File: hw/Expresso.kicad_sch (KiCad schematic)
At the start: 4 parts

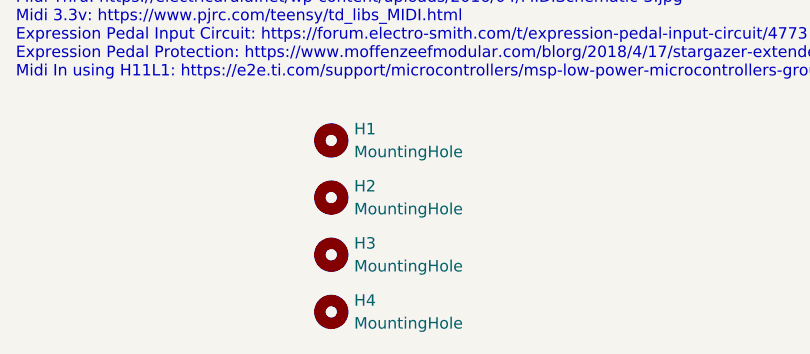
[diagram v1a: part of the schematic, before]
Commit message: added new pcb design, ERC errors not fixed yet
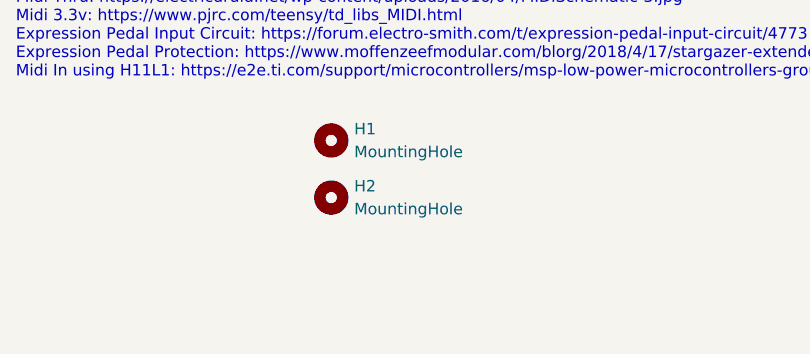
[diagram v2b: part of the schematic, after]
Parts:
- removed H3, H4: MountingHole, MountingHole:MountingHole_3.2mm_M3, symbol Mechanical:MountingHole
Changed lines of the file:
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@@
-	(symbol
-		(lib_id "Mechanical:MountingHole")
-		(at 50.8 190.5 0)
-		(unit 1)
-		(exclude_from_sim no)
-		(in_bom no)
-		(on_board yes)
-		(dnp no)
-		(fields_autoplaced yes)
-		(property "Reference" "H4"
-			(at 53.34 189.2299 0)
-			(effects
-				(font
-					(size 1.27 1.27)
-				)
-				(justify left)
-			)
-		)
-		(property "Value" "MountingHole"
-			(at 53.34 191.7699 0)
-			(effects
-				(font
-					(size 1.27 1.27)
-				)
-				(justify left)
-			)
-		)
-		(property "Footprint" "MountingHole:MountingHole_3.2mm_M3"
-			(at 50.8 190.5 0)
-			(effects
-				(font
-					(size 1.27 1.27)
-				)
-				(hide yes)
-			)
-		)
-		(property "Datasheet" "~"
-			(at 50.8 190.5 0)
-			(effects
-				(font
-					(size 1.27 1.27)
-				)
-				(hide yes)
-			)
-		)
-		(property "Description" "Mounting Hole without connection"
-			(at 50.8 190.5 0)
-			(effects
-				(font
-					(size 1.27 1.27)
-				)
-				(hide yes)
-			)
-		)
-		(instances
-			(project "Midi Expressor"
-				(path "/1e7cbae1-0003-4e27-ba62-2dd55b10f4f2"
-					(reference "H4")
-					(unit 1)
-				)
-			)
-		)
-	)
-	(symbol
-		(lib_id "Mechanical:MountingHole")
-		(at 50.8 184.15 0)
-		(unit 1)
-		(exclude_from_sim no)
-		(in_bom no)
-		(on_board yes)
-		(dnp no)
-		(fields_autoplaced yes)
-		(property "Reference" "H3"
-			(at 53.34 182.8799 0)
-			(effects
-				(font
-					(size 1.27 1.27)
-				)
-				(justify left)
-			)
-		)
-		(property "Value" "MountingHole"
-			(at 53.34 185.4199 0)
-			(effects
-				(font
-					(size 1.27 1.27)
-				)
-				(justify left)
-			)
-		)
-		(property "Footprint" "MountingHole:MountingHole_3.2mm_M3"
-			(at 50.8 184.15 0)
-			(effects
-				(font
-					(size 1.27 1.27)
-				)
-				(hide yes)
-			)
-		)
-		(property "Datasheet" "~"
-			(at 50.8 184.15 0)
-			(effects
-				(font
-					(size 1.27 1.27)
-				)
-				(hide yes)
-			)
-		)
-		(property "Description" "Mounting Hole without connection"
-			(at 50.8 184.15 0)
-			(effects
-				(font
-					(size 1.27 1.27)
-				)
-				(hide yes)
-			)
-		)
-		(instances
-			(project "Midi Expressor"
-				(path "/1e7cbae1-0003-4e27-ba62-2dd55b10f4f2"
-					(reference "H3")
-					(unit 1)
-				)
-			)
-		)
-	)
 	(symbol
 		(lib_id "Mechanical:MountingHole")

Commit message: small PCB updates for casing design
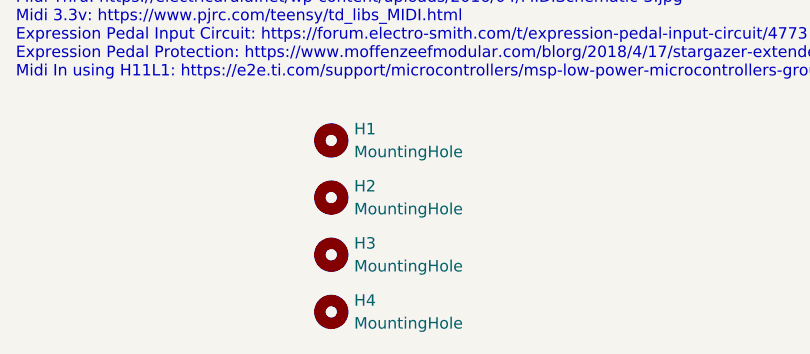
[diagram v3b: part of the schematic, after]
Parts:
- added H3, H4: MountingHole, MountingHole:MountingHole_3.2mm_M3, symbol Mechanical:MountingHole
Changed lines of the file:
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@@
+	(symbol
+		(lib_id "Mechanical:MountingHole")
+		(at 50.8 184.15 0)
+		(unit 1)
+		(exclude_from_sim no)
+		(in_bom no)
+		(on_board yes)
+		(dnp no)
+		(fields_autoplaced yes)
+		(property "Reference" "H3"
+			(at 53.34 182.8799 0)
+			(effects
+				(font
+					(size 1.27 1.27)
+				)
+				(justify left)
+			)
+		)
+		(property "Value" "MountingHole"
+			(at 53.34 185.4199 0)
+			(effects
+				(font
+					(size 1.27 1.27)
+				)
+				(justify left)
+			)
+		)
+		(property "Footprint" "MountingHole:MountingHole_3.2mm_M3"
+			(at 50.8 184.15 0)
+			(effects
+				(font
+					(size 1.27 1.27)
+				)
+				(hide yes)
+			)
+		)
+		(property "Datasheet" "~"
+			(at 50.8 184.15 0)
+			(effects
+				(font
+					(size 1.27 1.27)
+				)
+				(hide yes)
+			)
+		)
+		(property "Description" "Mounting Hole without connection"
+			(at 50.8 184.15 0)
+			(effects
+				(font
+					(size 1.27 1.27)
+				)
+				(hide yes)
+			)
+		)
+		(instances
+			(project "Expresso"
+				(path "/1e7cbae1-0003-4e27-ba62-2dd55b10f4f2"
+					(reference "H3")
+					(unit 1)
+				)
+			)
+		)
+	)
 	(symbol
 		(lib_id "Mechanical:MountingHole")
@@
 					(unit 1)
 				)
+			)
+		)
+	)
+	(symbol
+		(lib_id "Mechanical:MountingHole")
+		(at 50.8 190.5 0)
+		(unit 1)
+		(exclude_from_sim no)
+		(in_bom no)
+		(on_board yes)
+		(dnp no)
+		(fields_autoplaced yes)
+		(property "Reference" "H4"
+			(at 53.34 189.2299 0)
+			(effects
+				(font
+					(size 1.27 1.27)
+				)
+				(justify left)
+			)
+		)
+		(property "Value" "MountingHole"
+			(at 53.34 191.7699 0)
+			(effects
+				(font
+					(size 1.27 1.27)
+				)
+				(justify left)
+			)
+		)
+		(property "Footprint" "MountingHole:MountingHole_3.2mm_M3"
+			(at 50.8 190.5 0)
+			(effects
+				(font
+					(size 1.27 1.27)
+				)
+				(hide yes)
+			)
+		)
+		(property "Datasheet" "~"
+			(at 50.8 190.5 0)
+			(effects
+				(font
+					(size 1.27 1.27)
+				)
+				(hide yes)
+			)
+		)
+		(property "Description" "Mounting Hole without connection"
+			(at 50.8 190.5 0)
+			(effects
+				(font
+					(size 1.27 1.27)
+				)
+				(hide yes)
+			)
+		)
+		(instances
+			(project "Expresso"
+				(path "/1e7cbae1-0003-4e27-ba62-2dd55b10f4f2"
+					(reference "H4")
+					(unit 1)
+				)
